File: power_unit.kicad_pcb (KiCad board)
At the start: 2 copper layers, 100 x 100 mm, 54 parts, among them J1 ATX-20, U1 LM7805_TO220, U2 LM7905_TO220, X1 Power, X2 Address, X3 Data, X4 Mode, X5 Control, X6 Clock, X7 Power SW, X8 Reset SW, X9 Power LED

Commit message: Add files via upload
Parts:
- moved H1 1.00 mm to (66.7, 63.7)
- moved H2 1.00 mm to (157.7, 153.7)
- moved H3 1.00 mm to (66.7, 153.7)
- moved H4 1.00 mm to (157.7, 63.7)
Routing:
- net +12: track 60.4 -> 57.2 mm
- net Net-(JP1-A): track 61.5 -> 62.5 mm
- net GND: vias 367 -> 361

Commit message: Add files via upload
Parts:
- added X10: RTC Standby, Connector_PinSocket_2.54mm:PinSocket_1x02_P2.54mm_Vertical, F.Cu at (142.7, 129.6)
- J1: footprint Connector_Molex:Molex_Mini-Fit_Jr_5566-20A_2x10_P4.20mm_Vertical -> Connector_Molex:Molex_Mini-Fit_Jr_5566-20A2_2x10_P4.20mm_Vertical
- moved X6 4.98 mm to (97.0, 129.6)
- moved X9 2.51 mm to (152.2, 145.5)
- moved R8 1.53 mm to (144.2, 137.5)
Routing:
- net Net-(X9-Pin_1): track 9.67 -> 11.4 mm
- net +5: track 83.9 -> 82.4 mm
- net GND: vias 361 -> 852
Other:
- board text added: "+5VSB"
- board text added: "v.1.1 17/03/2026"
- board text removed: "v.1.0 29/01/2026"

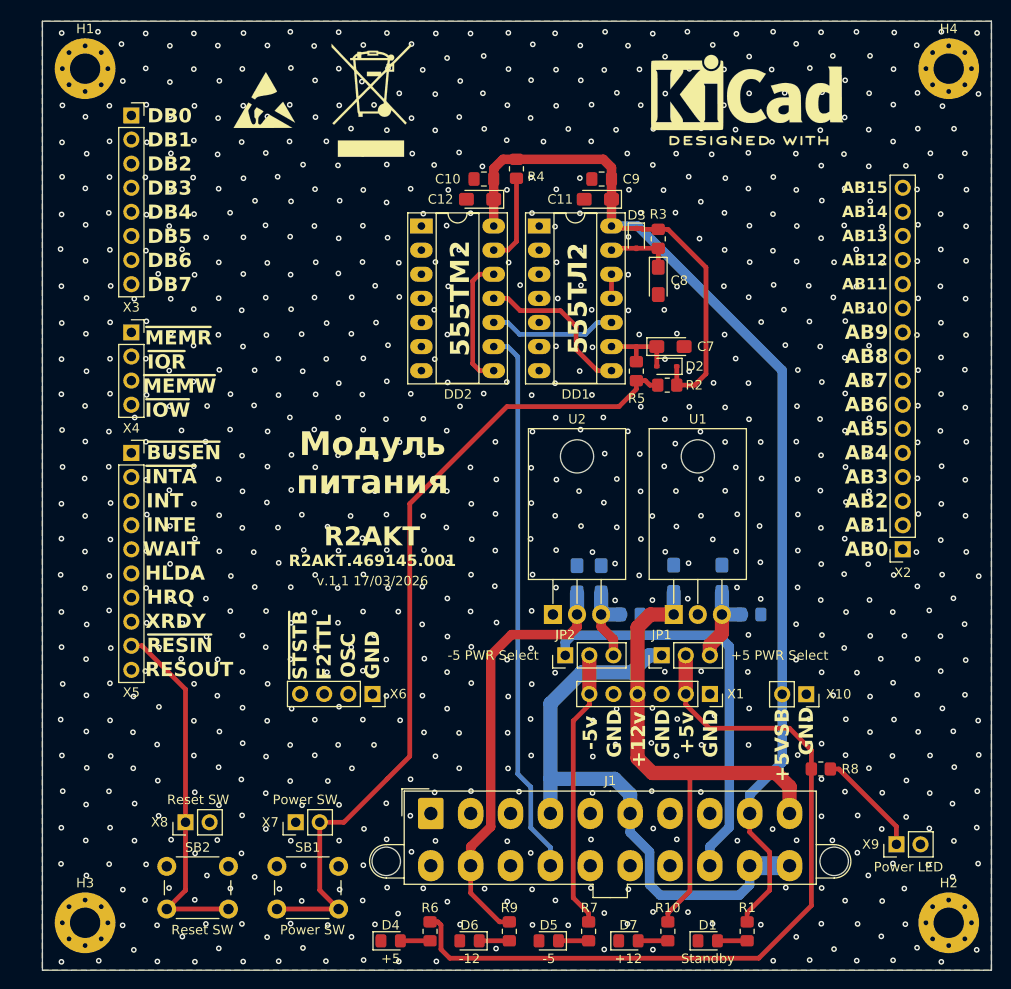
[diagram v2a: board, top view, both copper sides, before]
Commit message: Add files via upload
Removed +5V LVR, added connection 'PG_OK' to 'ResIn'.

Удалён линейный стабилизатор +5В, добавлено соединение 'PG_OK' с 'ResIn'.
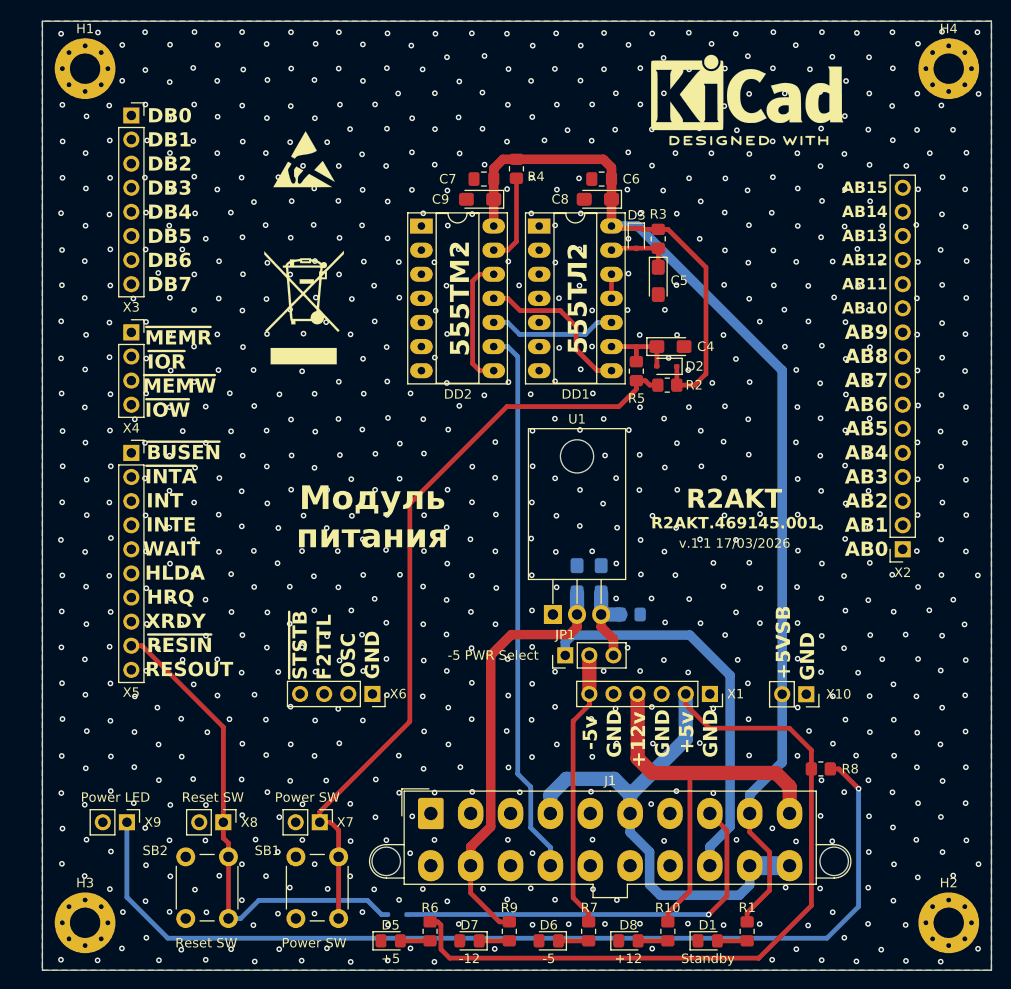
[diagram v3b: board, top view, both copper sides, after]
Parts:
- removed the C1 at (128.7, 117.5)
- removed the C2 at (136.9, 121.2)
- removed the C3 at (133.8, 117.5)
- removed the JP1 at (127.5, 125.5)
- removed the U1 at (128.7, 121.2)
- added D4: 1N4148WS, Diode_SMD:D_SOD-323, B.Cu at (99.6, 152.9)
- moved X9 81.1 mm to (71.1, 143.1), turned to -90 degrees
- moved REF** 23.0 mm to (89.8, 88.9)
- moved REF** 7.51 mm to (89.8, 73.2)
- moved SB1 5.85 mm to (88.9, 153.3), turned to 90 degrees
- moved SB2 5.85 mm to (77.3, 153.3), turned to 90 degrees
- moved X8 3.99 mm to (81.3, 143.1), turned to -90 degrees
- moved X7 2.54 mm to (91.4, 143.1), turned to -90 degrees
- renumbered C4 to C1, C5 to C2, C6 to C3, C7 to C4, C8 to C5, C9 to C6, C10 to C7, C11 to C8, C12 to C9, D4 to D5, D5 to D6, D6 to D7, D7 to D8, JP2 to JP1, U2 to U1
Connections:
- J1 pad 19: Net-(JP1-A) -> +5
- J1 pad 20: Net-(JP1-A) -> +5
- J1 pad 4: Net-(JP1-A) -> +5
- J1 pad 6: Net-(JP1-A) -> +5
- J1 pad 8: /~{ACLO} -> /PWR_OK
- R2 pad 1: Net-(X7-Pin_2) -> Net-(X7-Pin_1)
- R5 pad 1: Net-(X7-Pin_2) -> Net-(X7-Pin_1)
- SB1 pad 2: Net-(X7-Pin_2) -> Net-(X7-Pin_1)
- X7 pad 1: GND -> Net-(X7-Pin_1)
- X7 pad 2: Net-(X7-Pin_2) -> GND
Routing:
- net Net-(X9-Pin_1): track 11.4 -> 104.4 mm, vias 0 -> 1
- net Net-(X7-Pin_2): track 87.7 -> 0.00 mm
- net Net-(X7-Pin_1): track 0.00 -> 81.4 mm
- net Net-(JP1-A): track 62.5 -> 0.00 mm
- net +5: track 82.4 -> 131.1 mm
- net /PWR_OK: track 0.00 -> 44.0 mm, vias 0 -> 1
- net +12: track 57.2 -> 43.5 mm
- net /~{RESIN}: track 38.1 -> 51.8 mm
- net Net-(JP1-B) (its old number): track 9.19 -> 0.00 mm
- net Net-(J1--5V/NC): track 43.4 -> 41.8 mm
- net GND: vias 852 -> 853

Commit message: Update
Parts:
- added C4: 100u, Capacitor_Tantalum_SMD:CP_EIA-3528-21_Kemet-B_Pad1.50x2.35mm_HandSolder, F.Cu at (135.4, 96.6)
- added C5: 100n, Capacitor_SMD:C_0805_2012Metric_Pad1.18x1.45mm_HandSolder, F.Cu at (142.8, 75.5)
- added C6: 100u, Capacitor_Tantalum_SMD:CP_EIA-3528-21_Kemet-B_Pad1.50x2.35mm_HandSolder, F.Cu at (138.9, 96.6)
- added C7: 1u, Capacitor_Tantalum_SMD:CP_EIA-3216-18_Kemet-A_Pad1.58x1.35mm_HandSolder, F.Cu at (143.2, 77.6)
- added DD3: 1006ВИ1 (LM555), Package_DIP:DIP-8_W7.62mm_Socket_LongPads, F.Cu at (134.1, 80.3)
- added R1: 1k, Resistor_SMD:R_0805_2012Metric_Pad1.20x1.40mm_HandSolder, F.Cu at (98.6, 87.9)
- added R2: 1k, Resistor_SMD:R_0805_2012Metric_Pad1.20x1.40mm_HandSolder, F.Cu at (144.7, 96.6)
- added R3: 470, Resistor_SMD:R_0805_2012Metric_Pad1.20x1.40mm_HandSolder, F.Cu at (136.5, 154.6)
- added R8: 10k, Resistor_SMD:R_0805_2012Metric_Pad1.20x1.40mm_HandSolder, F.Cu at (137.9, 91.5)
- added VD1: 1N4148WS, Diode_SMD:D_SOD-323_HandSoldering, F.Cu at (99.5, 95.8)
- added VD2: 1N4148WS, Diode_SMD:D_SOD-323_HandSoldering, F.Cu at (99.5, 91.7)
- added VD3: CPU Act, LED_SMD:LED_0805_2012Metric_Pad1.15x1.40mm_HandSolder, F.Cu at (132.3, 155.6)
- added VT1: MMBT2222A, Package_TO_SOT_SMD:SOT-23_Handsoldering, F.Cu at (143.7, 92.4)
- added X7: Conn_01x10, Connector_PinHeader_2.54mm:PinHeader_1x10_P2.54mm_Vertical, F.Cu at (147.8, 68.6)
- J1: footprint Connector_Molex:Molex_Mini-Fit_Jr_5566-20A2_2x10_P4.20mm_Vertical -> Library:ATX-20
- R12: renamed from R8; moved to B.Cu
- VD4: renamed from D2; footprint Diode_SMD:D_SOD-323 -> Diode_SMD:D_SOD-323_HandSoldering
- VD5: renamed from D3; footprint Diode_SMD:D_SOD-323 -> Diode_SMD:D_SOD-323_HandSoldering
- moved REF** 34.4 mm to (102.1, 64.7)
- moved J1 19.0 mm to (122.1, 144.4)
- moved R12 15.5 mm to (140.9, 152.6), turned to -90 degrees
- moved R9 8.37 mm to (144.8, 154.6)
- moved VD6 8.35 mm to (140.7, 155.6)
- moved REF** 7.04 mm to (89.7, 80.3)
- moved REF** 6.65 mm to (89.7, 95.5)
- moved C8 4.77 mm to (124.8, 89.9), turned to 90 degrees
- moved VD4 2.09 mm to (128.2, 93.0)
- moved R4 0.62 mm to (128.4, 96.6)
- moved C9 0.22 mm to (127.1, 86.3)
- moved R5 0.19 mm to (127.1, 81.8)
- renumbered C6 to C10, C7 to C11, C8 to C12, C9 to C13, C4 to C8, C5 to C9, U1 to DA1, R6 to R10, R7 to R11, R9 to R13, R10 to R14, R2 to R4, R3 to R5, R4 to R6, R5 to R7, R1 to R9, D8 to VD10, D4 to VD11, D1 to VD6, D5 to VD7, D6 to VD8, D7 to VD9, X9 to X10, X10 to X11, X7 to X8, X8 to X9
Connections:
- net /INTE renamed /~{WRQ}
- net /Single_BCLK renamed /F2TTL
- net /Single_OSC_TTL renamed /OSC_TTL
- DD1 pad 1: GND -> Net-(DD2B-D)
- DD1 pad 2: unconnected-(DD1-Pad2) -> Net-(DD3-R)
- DD1 pad 5: GND -> /~{PS_ON}
- DD1 pad 6: unconnected-(DD1-Pad6) -> Net-(VD1-K)
- DD2 pad 1: GND -> /+5VSB
- DD2 pad 2: GND -> Net-(DD2A-D)
- DD2 pad 3: GND -> Net-(DD2A-C)
- DD2 pad 4: GND -> /+5VSB
- DD2 pad 5: unconnected-(DD2A-Q-Pad5) -> Net-(DD2A-Q)
- DD2 pad 6: unconnected-(DD2A-~{Q}-Pad6) -> Net-(DD2A-D)
- R9 pad 1: /+5VSB -> Net-(VT1-E)
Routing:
- net Net-(VD1-A): track 0.00 -> 110.6 mm, vias 0 -> 2
- net Net-(VT1-E): track 0.00 -> 63.7 mm, vias 0 -> 2
- net Net-(DD2A-C): track 0.00 -> 53.5 mm, vias 0 -> 2
- net /+5VSB: track 139.5 -> 175.3 mm
- net Net-(DD3-THR): track 0.00 -> 25.7 mm
- net Net-(X10-Pin_1): track 104.4 -> 80.7 mm, vias 1 -> 0
- net Net-(DD3-R): track 0.00 -> 21.7 mm
- net Net-(VD1-K): track 0.00 -> 18.6 mm
- net +5: track 131.1 -> 114.6 mm
- net Net-(DD2A-D): track 0.00 -> 14.3 mm
- net Net-(DD2B-D): track 13.7 -> 22.6 mm
- net Net-(DD3-Q): track 0.00 -> 8.13 mm
- net /AB7: track 0.00 -> 7.13 mm
- net /~{PS_ON}: track 58.0 -> 63.9 mm
- net /PWR_OK: track 44.0 -> 38.8 mm, vias 1 -> 0
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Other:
- board text added: "1006ВИ1"
- board text added: "IRQ0"
- board text added: "IRQ1"
- board text added: "IRQ2"
- board text added: "IRQ3"
- board text added: "IRQ4"
- board text added: "IRQ5"
- board text added: "IRQ6"
- board text added: "IRQ7"
- board text added: "v.1.2 14/04/2026"
- board text added: "~{WRQ}"
- board text removed: "INTE"
- board text removed: "v.1.1 17/03/2026"

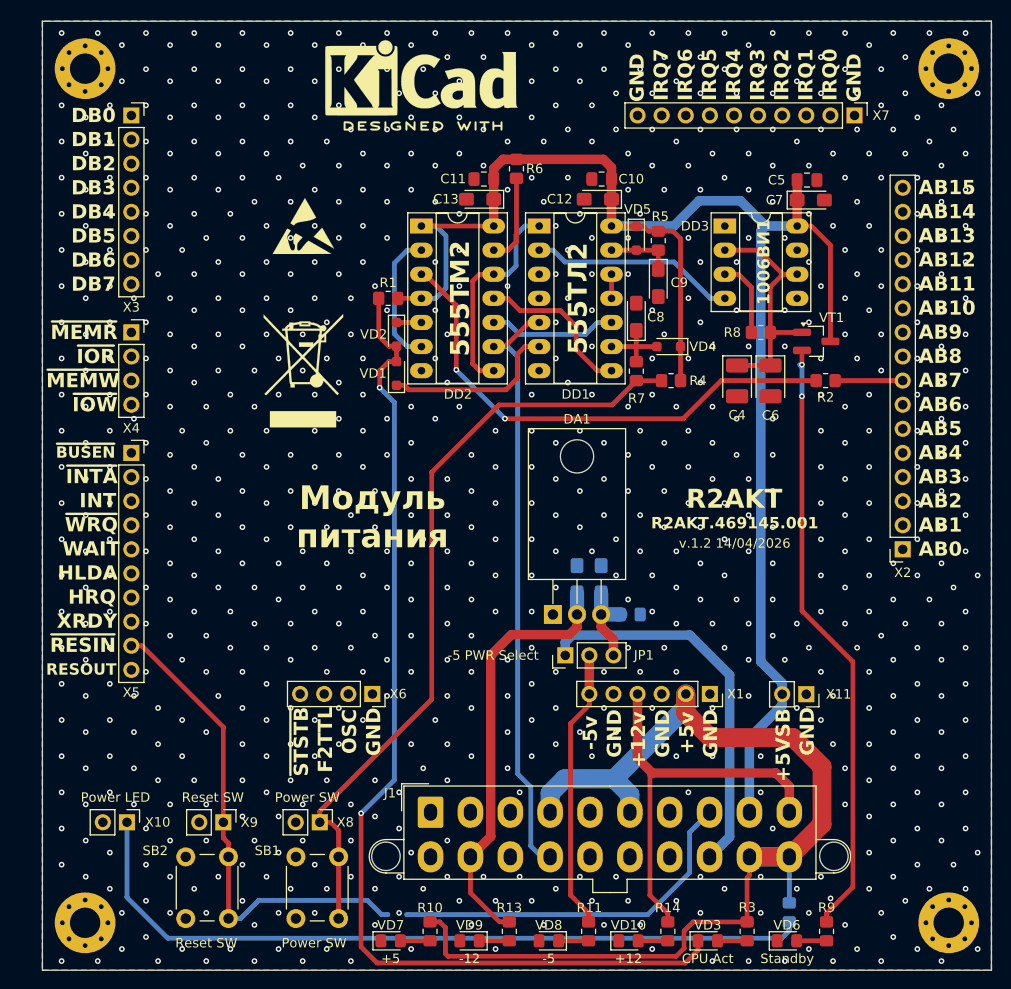
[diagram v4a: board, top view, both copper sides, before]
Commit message: Update
Fix footprint's, change optional shematic, add comment's
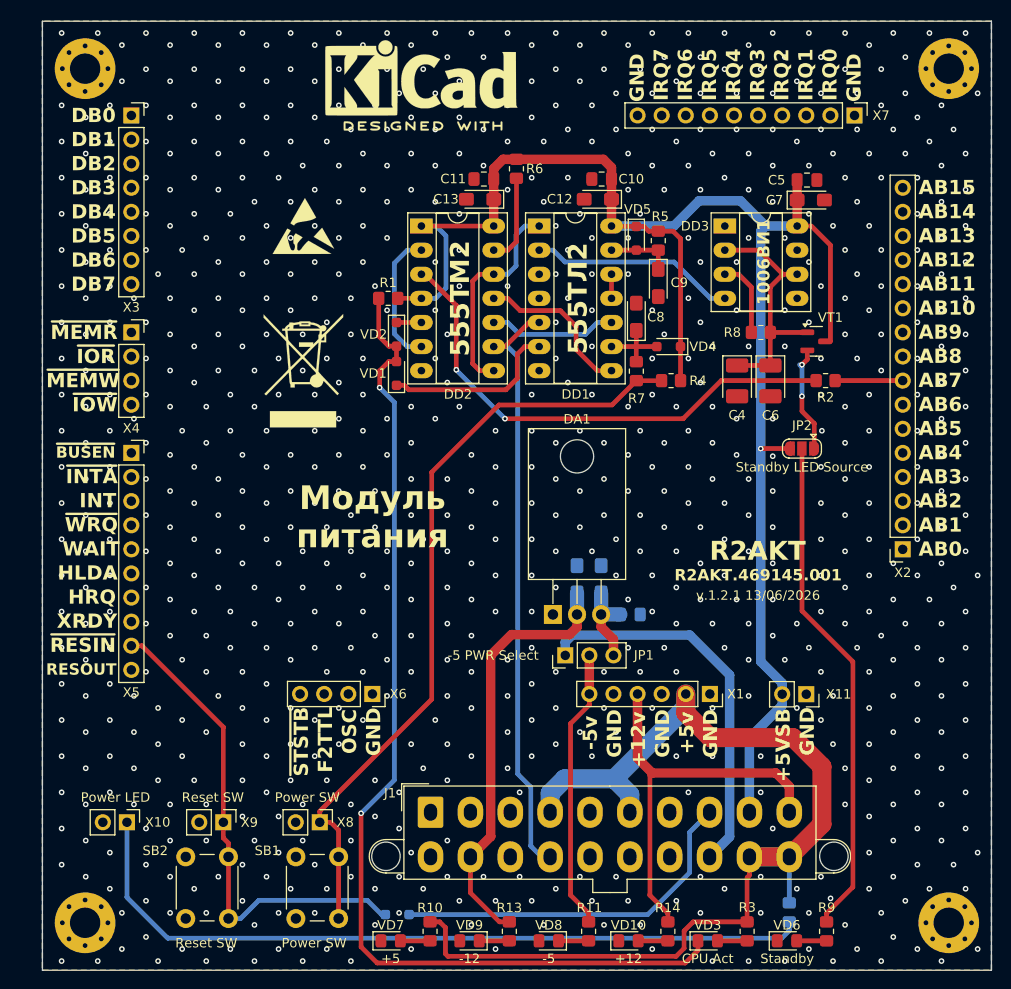
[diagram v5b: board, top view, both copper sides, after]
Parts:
- added JP2: Standby LED Source, Jumper:SolderJumper-3_P1.3mm_Open_RoundedPad1.0x1.5mm, F.Cu at (142.2, 103.8)
- C6: value 100u -> 100u*
- VD11: footprint Diode_SMD:D_SOD-323 -> Diode_SMD:D_SOD-323_HandSoldering
- VT1: footprint Package_TO_SOT_SMD:SOT-23_Handsoldering -> Package_TO_SOT_SMD:SOT-23
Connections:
- R9 pad 1: Net-(VT1-E) -> Net-(JP2-C)
- VT1 pad 2: Net-(VT1-E) -> Net-(JP2-A)
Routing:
- net Net-(VT1-E): track 63.7 -> 0.00 mm, vias 2 -> 0
- net Net-(JP2-C): track 0.00 -> 53.2 mm
- net Net-(JP2-A): track 0.00 -> 11.2 mm, vias 0 -> 2
- net /+5VSB: track 175.3 -> 178.4 mm, vias 0 -> 1
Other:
- board text added: "v.1.2.1 13/06/2026"
- board text removed: "v.1.2 14/04/2026"
